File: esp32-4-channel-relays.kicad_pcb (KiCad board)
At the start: 2 copper layers, 76 x 76.6 mm, 59 parts, among them J1 Relay-1, J2 Relay-2, J3 Relay-3, J4 Relay-4, K1 SRD-05VDC-SL-C, K2 SRD-05VDC-SL-C, K3 SRD-05VDC-SL-C, K4 SRD-05VDC-SL-C, Q1 MBT3904DW1, Q2 BC547A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

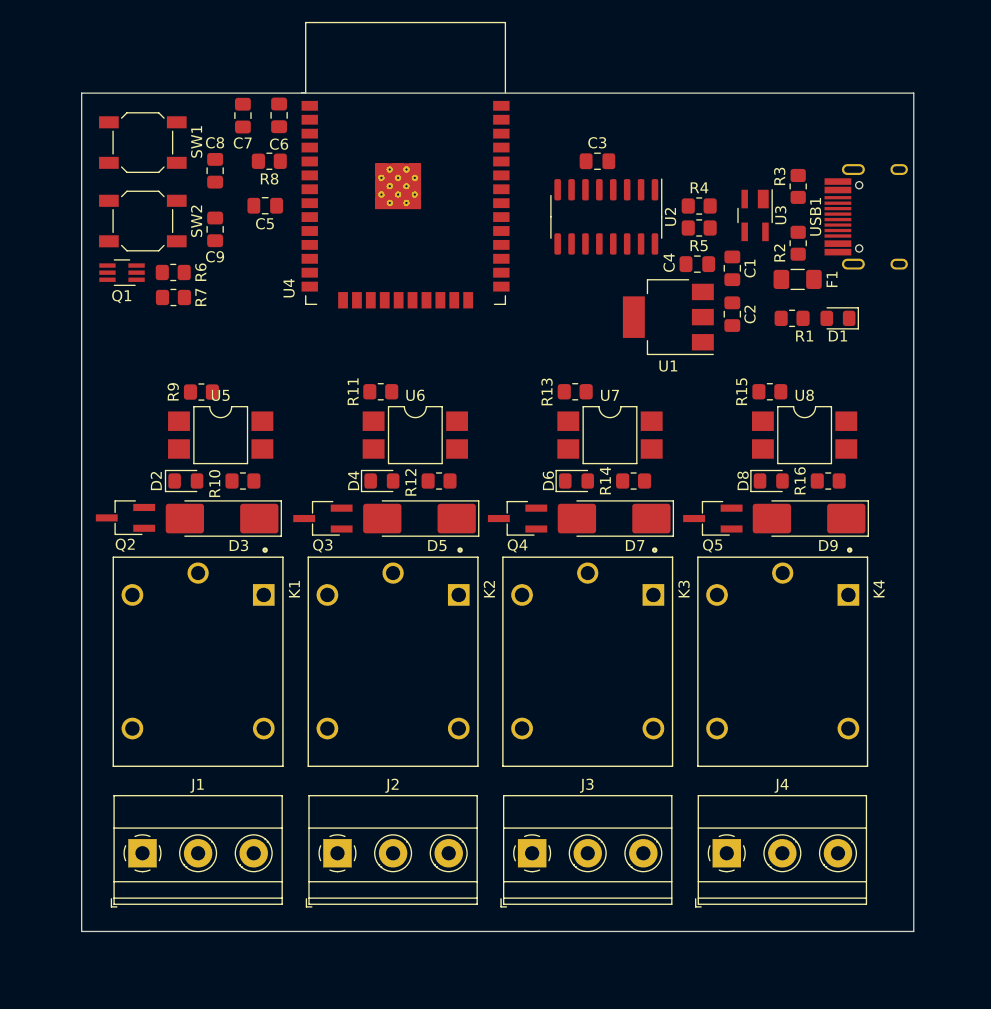
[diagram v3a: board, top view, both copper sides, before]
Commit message: Add mounting hole to pcb editor and redraw edgecut
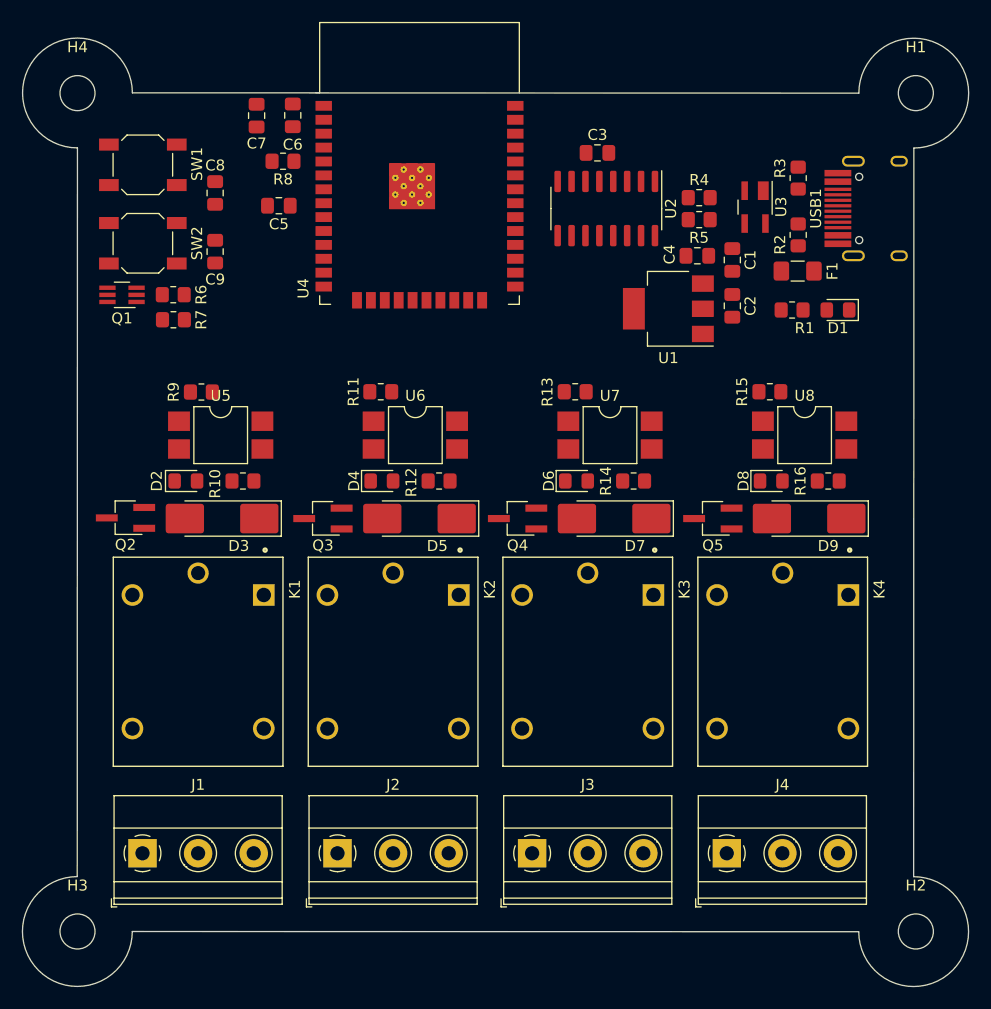
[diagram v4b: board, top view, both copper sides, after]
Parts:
- added H1: MountingHole, MountingHole:MountingHole_3.2mm_M3, F.Cu at (203.2, 53.6)
- added H2: MountingHole, MountingHole:MountingHole_3.2mm_M3, F.Cu at (203.2, 130.2)
- added H3: MountingHole, MountingHole:MountingHole_3.2mm_M3, F.Cu at (126.6, 130.2)
- added H4: MountingHole, MountingHole:MountingHole_3.2mm_M3, F.Cu at (126.6, 53.6)
- moved C8 2.03 mm to (139.2, 62.7)
- moved SW1 2.03 mm to (132.6, 60.1)
- moved C9 2.03 mm to (139.2, 68.1)
- moved Q1 2.03 mm to (130.7, 72.0)
- moved R6 2.03 mm to (135.4, 72.0)
- moved R7 2.03 mm to (135.4, 74.3)
- moved SW2 2.03 mm to (132.6, 67.3)
- moved U4 1.27 mm to (157.9, 63.0)
- moved C6 1.25 mm to (146.3, 55.6)
- moved C7 1.25 mm to (143.0, 55.6)
- moved C5 1.25 mm to (145.0, 63.9)
- moved R8 1.25 mm to (145.4, 59.8)
- moved C1 0.76 mm to (186.4, 68.8)
- moved C2 0.76 mm to (186.4, 73.0)
- moved C3 0.76 mm to (174.1, 59.1)
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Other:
- board size 76 x 76.6 mm -> 86.4 x 86.6 mm

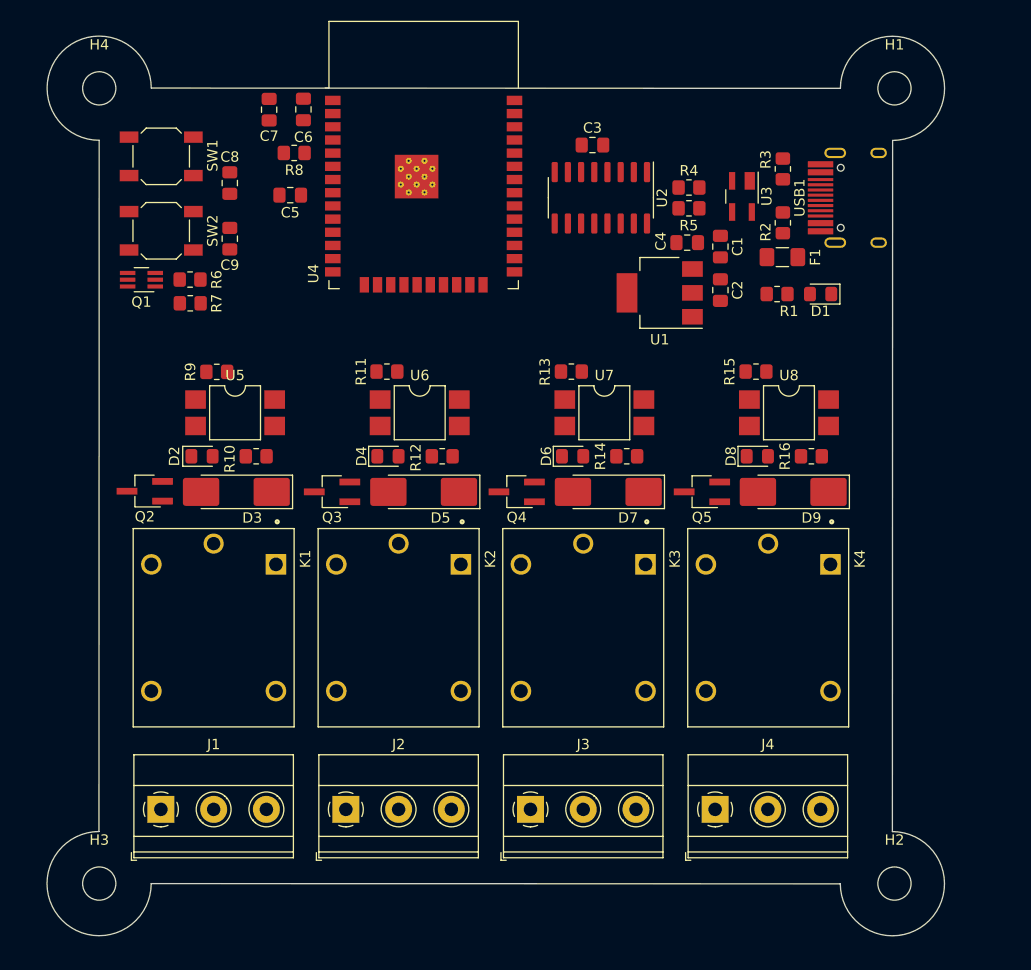
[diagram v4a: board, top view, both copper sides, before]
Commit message: Add fill zone and routing VCC, 5V and 3.3V power
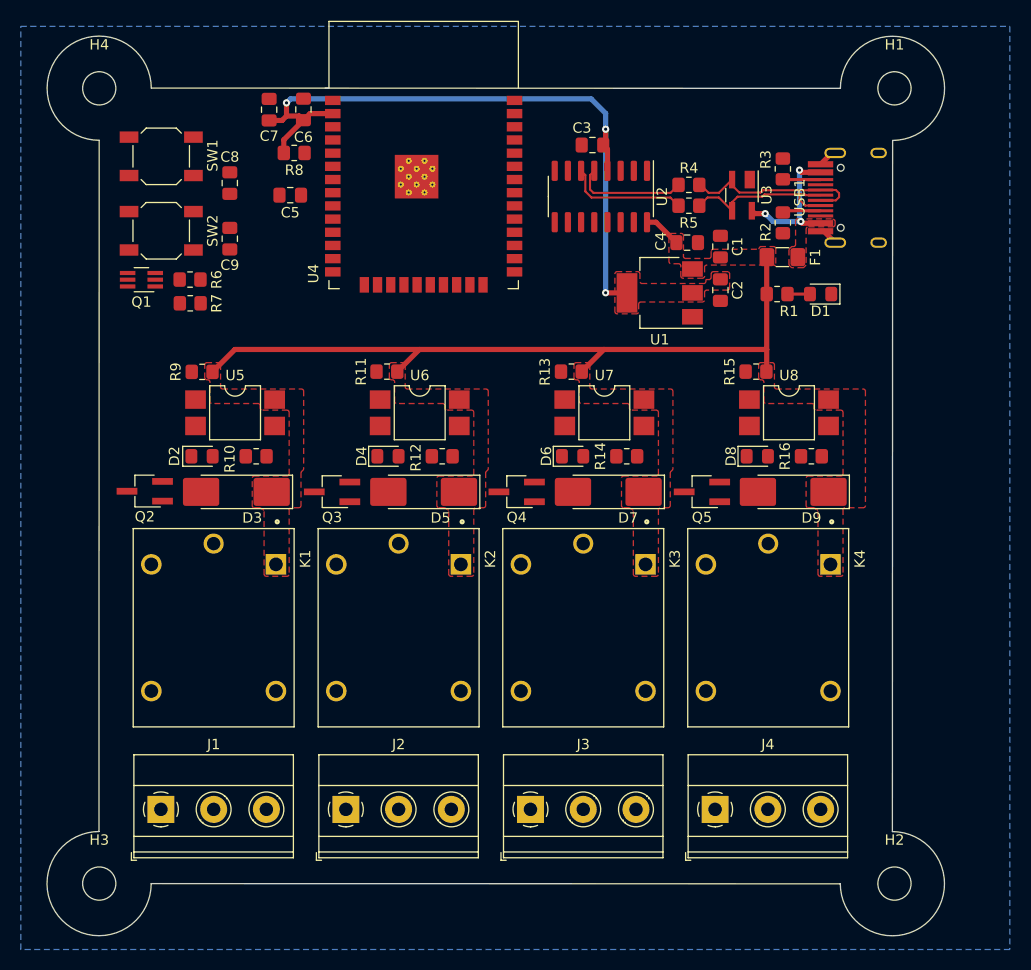
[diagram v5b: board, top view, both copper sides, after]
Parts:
- moved R9 1.41 mm to (136.5, 80.9)
- moved R4 0.25 mm to (183.4, 62.9)
- moved R5 0.25 mm to (183.4, 64.9)
- moved U3 0.13 mm to (188.5, 63.9)
- moved U2 0.12 mm to (174.9, 64.0)
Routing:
- net +5V: track 0.00 -> 75.0 mm
- net +3.3V: track 0.00 -> 67.0 mm, vias 0 -> 3
- net /DP: track 0.00 -> 17.1 mm
- net /DN: track 0.00 -> 16.5 mm
- net VCC: track 0.00 -> 14.2 mm, vias 0 -> 3
- net /D-: track 0.00 -> 11.7 mm
- net /D+: track 0.00 -> 10.9 mm
- net GND: track 0.00 -> 3.74 mm
- net Net-(USB1-CC1): track 0.00 -> 3.70 mm
- net Net-(USB1-CC2): track 0.00 -> 3.64 mm
- net Net-(D1-A): track 0.00 -> 2.17 mm
- added copper zone on F.Cu, net +3.3V
- added copper zone on F.Cu, net +5V
- added copper zone on B.Cu, net GND
- added copper zone on F.Cu, net VCC

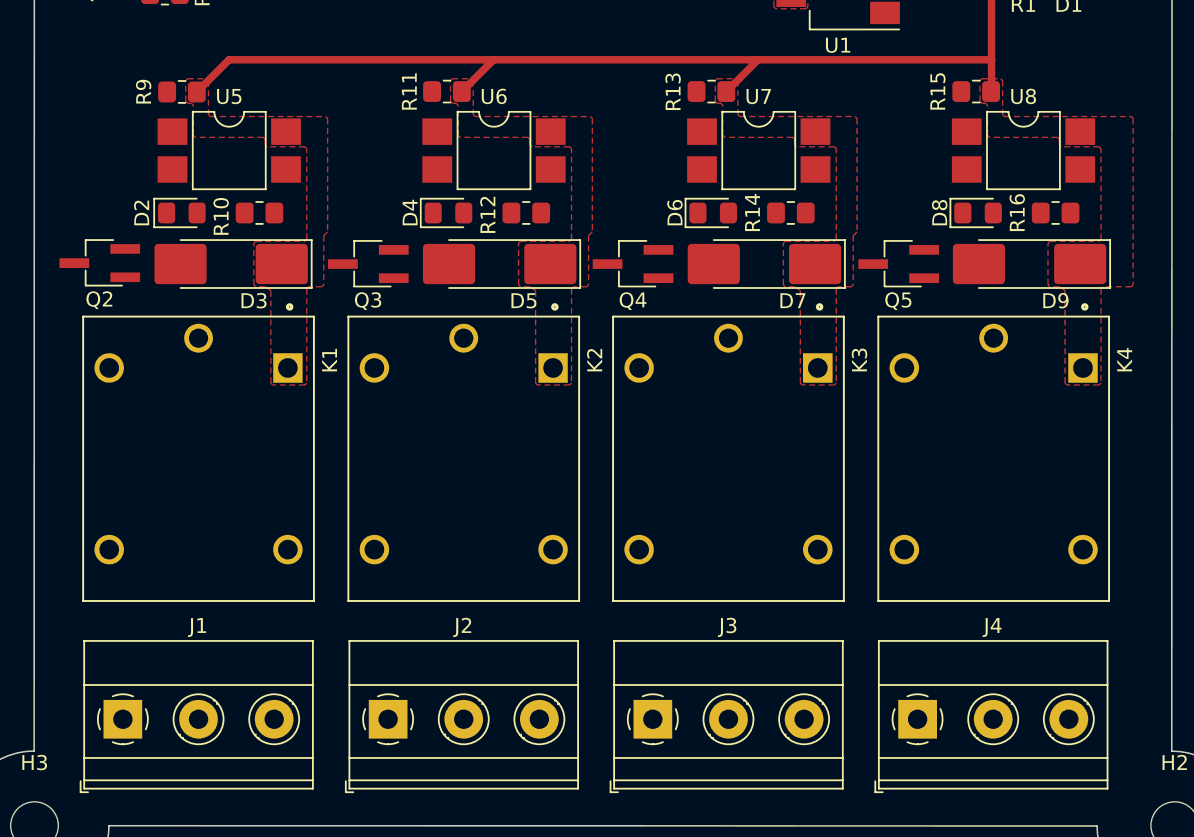
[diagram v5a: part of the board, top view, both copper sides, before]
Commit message: Routing relays
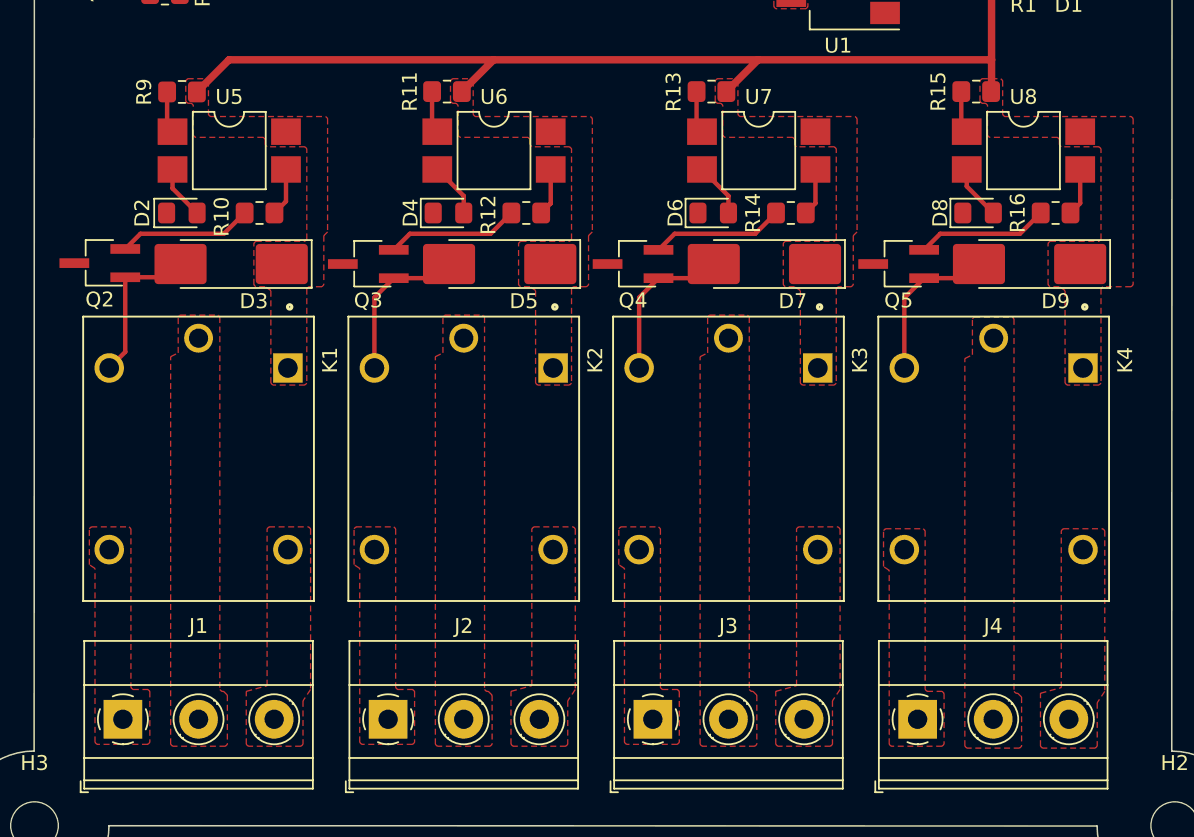
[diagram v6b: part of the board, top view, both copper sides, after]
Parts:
- turned R14 to 180 degrees
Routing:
- net Net-(D7-A): track 0.00 -> 10.7 mm
- net Net-(D5-A): track 0.00 -> 10.7 mm
- net Net-(D9-A): track 0.00 -> 10.7 mm
- net Net-(D3-A): track 0.00 -> 10.6 mm
- net Net-(Q2-B): track 0.00 -> 9.02 mm
- net Net-(Q3-B): track 0.00 -> 8.93 mm
- net Net-(Q4-B): track 0.00 -> 8.92 mm
- net Net-(Q5-B): track 0.00 -> 8.86 mm
- net Net-(D8-A): track 0.00 -> 3.66 mm
- net Net-(D6-A): track 0.00 -> 3.66 mm
- net Net-(D4-A): track 0.00 -> 3.66 mm
- net Net-(D2-A): track 0.00 -> 3.60 mm
- net Net-(R10-Pad1): track 0.00 -> 3.24 mm
- net Net-(R16-Pad1): track 0.00 -> 3.19 mm
- net Net-(R14-Pad1): track 0.00 -> 3.19 mm
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- added copper zone on F.Cu, net /COM-1
- added copper zone on F.Cu, net /COM-2
- added copper zone on F.Cu, net /COM-3
- added copper zone on F.Cu, net /COM-4
- added copper zone on F.Cu, net /NC-1
- added copper zone on F.Cu, net /NC-2
- added copper zone on F.Cu, net /NC-3
- added copper zone on F.Cu, net /NC-4
- added copper zone on F.Cu, net /NO-1
- added copper zone on F.Cu, net /NO-2
- added copper zone on F.Cu, net /NO-3
- added copper zone on F.Cu, net /NO-4
